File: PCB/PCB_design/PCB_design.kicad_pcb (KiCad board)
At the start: 2 copper layers, 67.4 x 80 mm, 55 parts, among them J1 Conn_01x01_Pin, J2 Conn_01x01_Pin, J3 Conn_01x01_Pin, J4 Conn_01x01_Pin, J5 Conn_01x01_Pin, J6 Conn_01x01_Pin, J7 Conn_02x04_Counter_Clockwise, J8 Conn_01x01_Pin, K1 Relay_SPST-NO, K2 Relay_SPST-NO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

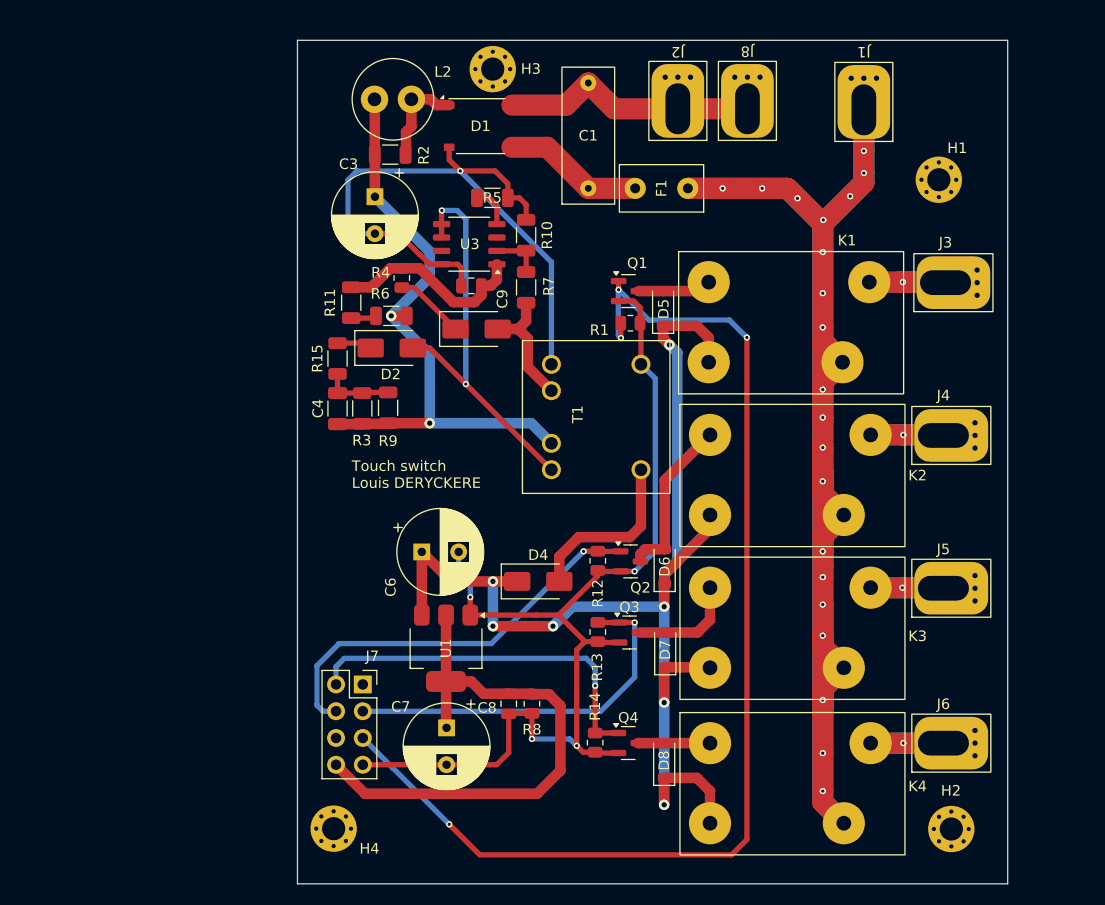
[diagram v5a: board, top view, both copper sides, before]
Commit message: Modif footprint relais & refaçonnage
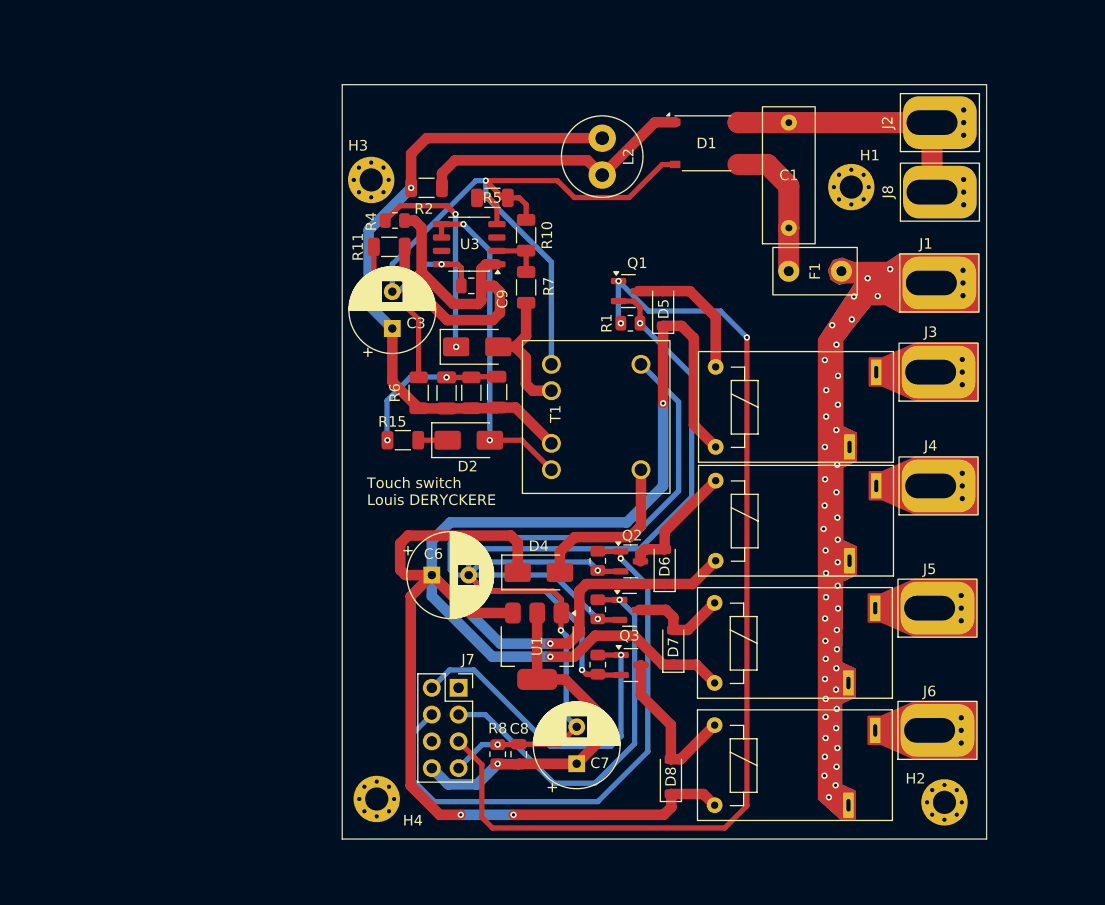
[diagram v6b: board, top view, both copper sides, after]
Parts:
- K1, K2, K3, K4: footprint Touch_Switch_Custom:FH17-1A2STLE-DC5V -> Touch_Switch_Custom:relay
- moved J2 24.2 mm to (157.2, 37.6), turned to 90 degrees
- moved D1 21.5 mm to (135.8, 39.6)
- moved L2 19.5 mm to (125.9, 42.6), turned to 90 degrees
- moved C1 19.4 mm to (143.6, 47.6)
- moved J8 19.2 mm to (157.2, 44.2), turned to 90 degrees
- moved J1 17.6 mm to (157.2, 52.8), turned to 90 degrees
- moved F1 16.6 mm to (146.1, 51.7)
- moved H3 15.6 mm to (104.0, 43.0)
- moved C7 12.8 mm to (123.5, 98.5), turned to 90 degrees
- moved C3 12.6 mm to (106.0, 57.2), turned to 90 degrees
- moved D2 11.4 mm to (113.2, 67.8)
- moved C4 10.5 mm to (111.2, 63.3)
- moved R9 10.5 mm to (116.0, 63.2)
- moved R3 10.5 mm to (113.5, 63.2)
- moved R15 9.92 mm to (107.0, 67.8), turned to 0 degrees
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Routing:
- net L: track 225.5 -> 0.00 mm, vias 21 -> 46
- net +5VDC: track 120.0 -> 208.6 mm, vias 7 -> 5
- net GND2: track 101.3 -> 176.8 mm, vias 4 -> 6
- net Net-(J3-Pin_1): track 24.9 -> 0.00 mm, vias 1 -> 0
- net +3.3V: track 52.0 -> 34.5 mm, vias 0 -> 1
- net Net-(D1-+): track 9.29 -> 26.7 mm
- net VCC_IC: track 18.8 -> 35.8 mm
- net CT2: track 39.1 -> 54.5 mm
- net Net-(J5-Pin_1): track 13.9 -> 0.00 mm, vias 1 -> 0
- net Net-(J4-Pin_1): track 13.9 -> 0.00 mm, vias 1 -> 0
- net Net-(J6-Pin_1): track 13.8 -> 0.00 mm, vias 1 -> 0
- net Net-(D3-K): track 6.73 -> 20.2 mm, vias 0 -> 2
- net Net-(R11-Pad1): track 2.44 -> 15.6 mm
- net CT1: track 110.3 -> 97.5 mm, vias 4 -> 3
- net Net-(D8-A): track 6.82 -> 15.6 mm
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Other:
- board size 67.4 x 80 mm -> 61.2 x 71.6 mm

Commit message: Modif vias
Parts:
- moved H3 4.77 mm to (104.2, 38.3)
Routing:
- net GND2: track 176.8 -> 137.8 mm, vias 6 -> 12
- net +5VDC: track 208.6 -> 214.9 mm, vias 5 -> 10
- net GND: track 70.4 -> 66.4 mm, vias 2 -> 4
- net +3.3V: track 34.5 -> 38.0 mm, vias 1 -> 2
- net CT2: track 54.5 -> 53.6 mm, vias 1 -> 2
- net CT1: track 97.5 -> 98.4 mm, vias 3 -> 6
- net +310VDC: track 60.6 -> 61.4 mm, vias 1 -> 2
- net CT4: track 32.0 -> 31.4 mm, vias 1 -> 2
- net CT3: track 37.3 -> 36.8 mm, vias 1 -> 2
- net Net-(D3-K): track 20.2 -> 20.6 mm, vias 2 -> 4
- net C: track 31.9 -> 31.7 mm, vias 2 -> 4
- net Net-(C4-Pad2): track 15.2 -> 15.3 mm, vias 2 -> 4
